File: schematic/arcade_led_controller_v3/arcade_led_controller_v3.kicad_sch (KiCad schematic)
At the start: 48 parts, among them J4 Pico_Socket_Row_2, J5 Pico_Socket_Row_1, Q1 Q_NMOS_GDS, Q2 Q_NMOS_GDS, Q3 Q_NMOS_GDS, Q4 Q_NMOS_GDS, Q5 Q_NMOS_GDS, Q6 Q_NMOS_GDS, Q7 Q_NMOS_GDS, Q8 Q_NMOS_GDS, U1 74AHCT125, U2 74AHCT125, U3 74AHCT125, U4 74AHCT125

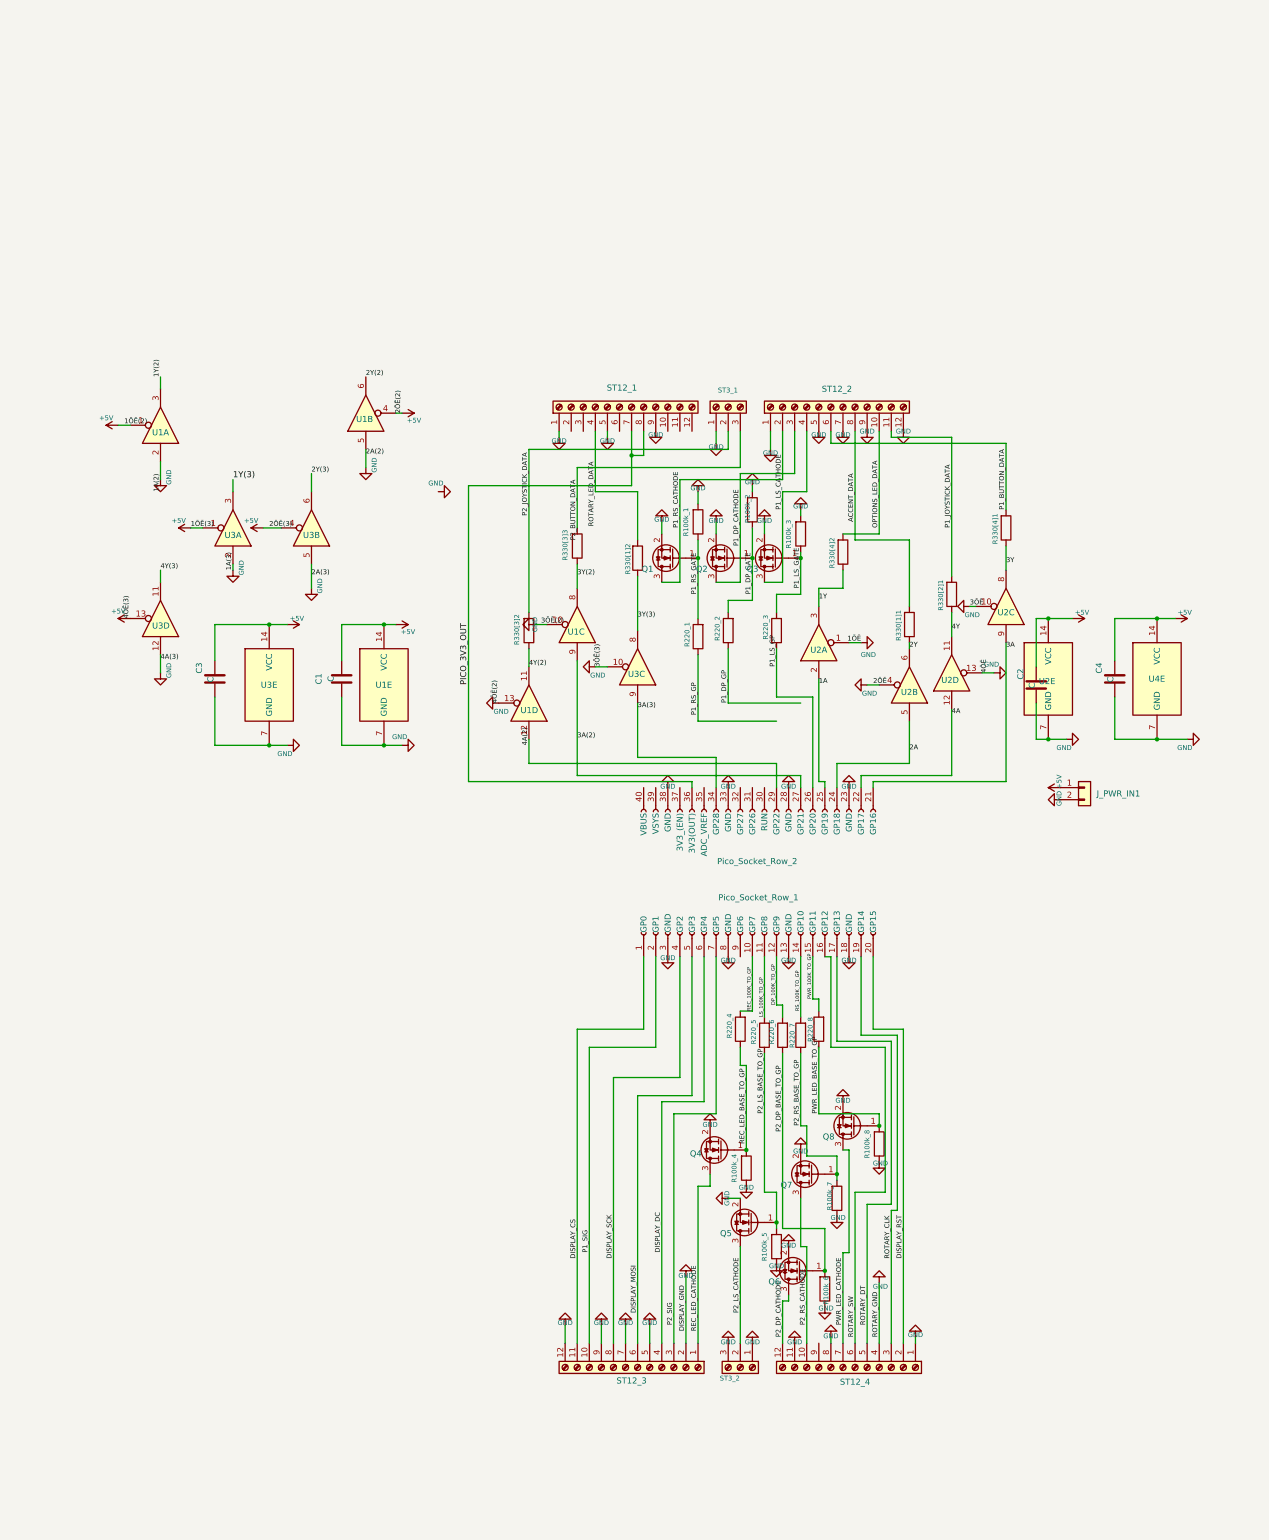
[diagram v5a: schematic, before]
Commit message: complete routing
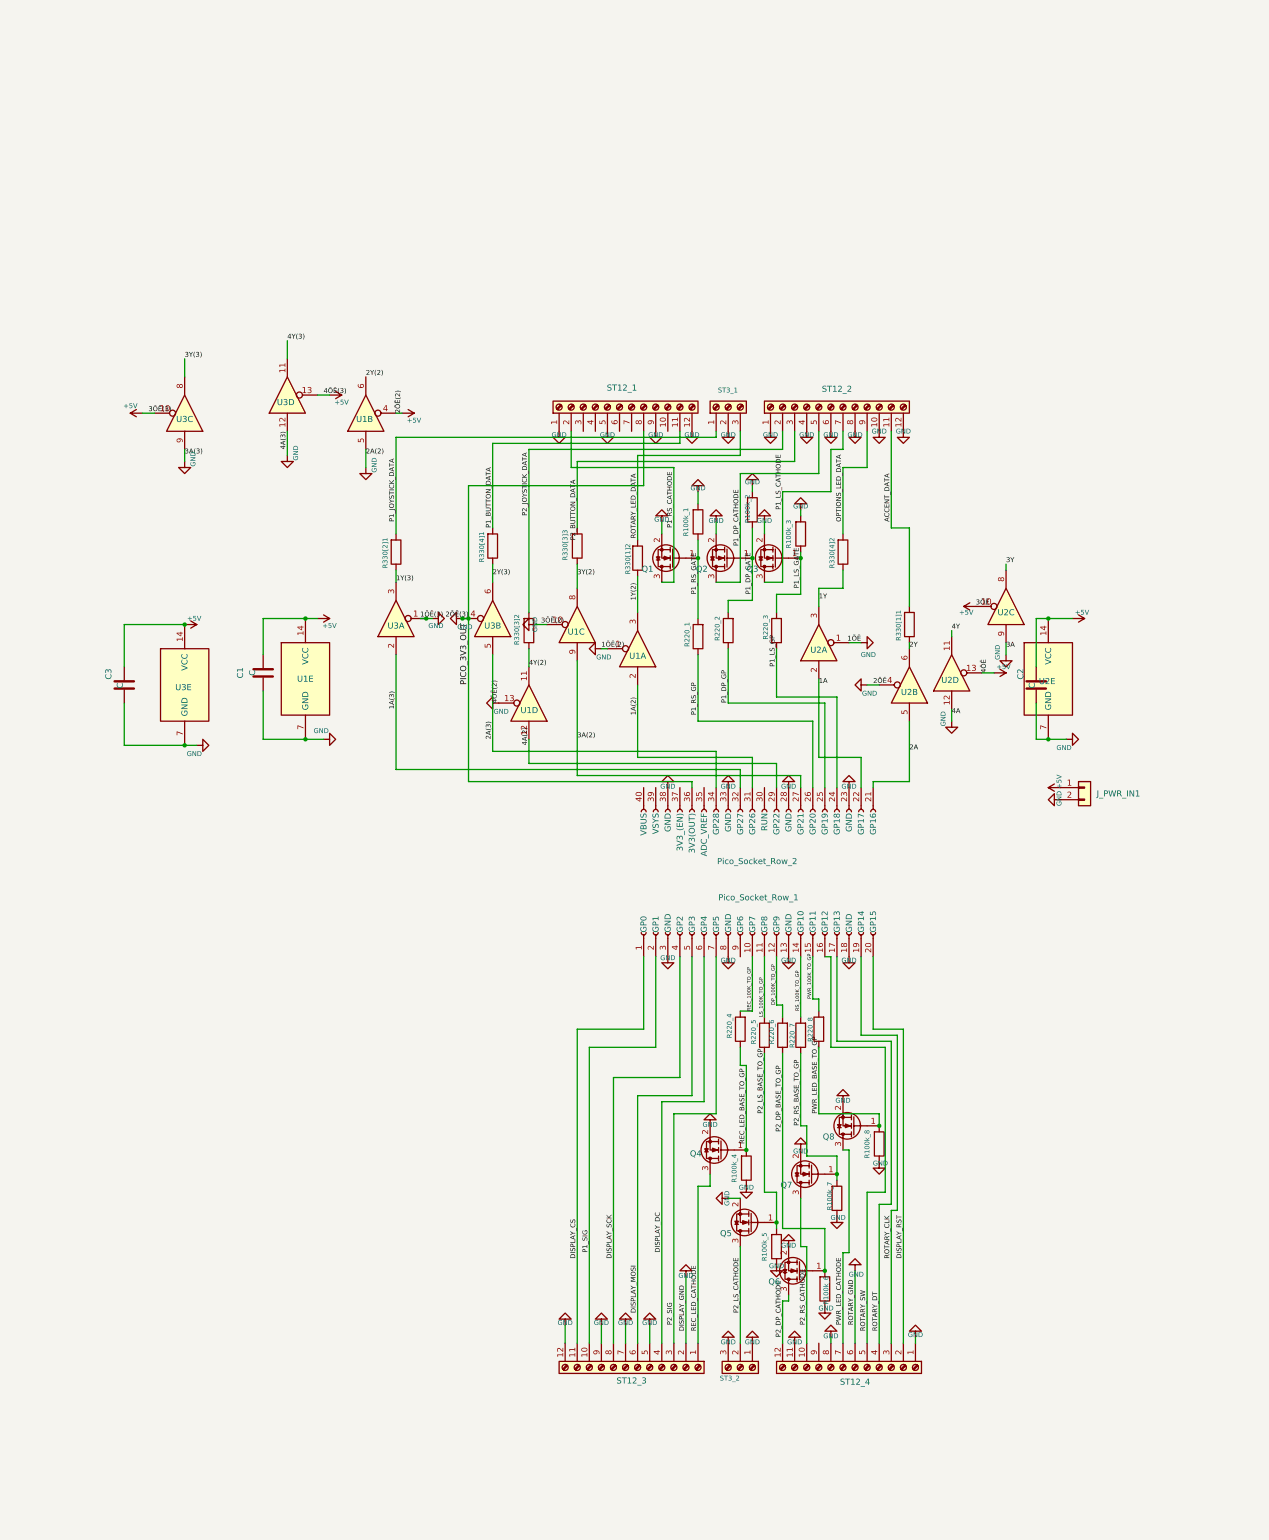
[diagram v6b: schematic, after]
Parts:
- removed C4: C, Capacitor_SMD:C_0805_2012Metric_Pad1.18x1.45mm_HandSolder, symbol Device:C
- removed U4: 74AHCT125, Package_SO:SOIC-14_3.9x8.7mm_P1.27mm, symbol 74xx:74AHCT125
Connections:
- net +5V: now also U2.10, U2.13, U3.10; no longer U1.1, U3.1, U3.4
- net 1A: now also J4.22 (GP17); no longer J4.25 (GP19)
- net 1Y(2): now also R330[1]2.1
- net 1Y(3): now also R330[2]1.1
- net 2A: now also J4.21 (GP16); no longer J4.24 (GP18)
- net 2Y(3): now also R330[4]1.1
- net 3Y: no longer R330[4]1.1
- net 3Y(3): no longer R330[1]2.1
- net 4Y: no longer R330[2]1.1
- net ACCENT_DATA: now also ST12_2.11 (Pin_11); no longer ST12_2.8 (Pin_8)
- net GND: now also J4.36 (3V3(OUT)), ST12_1.12 (Pin_12), ST12_1.8 (Pin_8), ST12_2.10 (Pin_10), ST12_2.4 (Pin_4), ST12_2.6 (Pin_6), ST12_2.8 (Pin_8), ST12_4.6 (Pin_6), ST3_1.2 (Pin_2), U1.1, U2.12, U2.9, U3.1, U3.4, U3.9; no longer ST12_2.5 (Pin_5), ST12_2.7 (Pin_7), ST12_2.9 (Pin_9), ST12_4.4 (Pin_4), ST3_1.1 (Pin_1), U1.2, U2.10, U2.13, U3.10, U3.2, U3.5
- net OPTIONS_LED_DATA: now also ST12_2.9 (Pin_9); no longer ST12_2.10 (Pin_10)
- net P1_BUTTON_DATA: now also ST12_1.11 (Pin_11); no longer ST12_2.6 (Pin_6)
- net P1_DP_CATHODE: now also ST12_2.5 (Pin_5); no longer ST12_2.3 (Pin_3)
- net P1_DP_GP: now also J4.25 (GP19)
- net P1_JOYSTICK_DATA: now also ST3_1.1 (Pin_1); no longer ST12_2.11 (Pin_11)
- net P1_LS_CATHODE: now also ST12_2.7 (Pin_7); no longer ST12_2.4 (Pin_4)
- net P1_LS_GP: now also J4.24 (GP18); no longer J4.26 (GP20)
- net P1_RS_CATHODE: now also ST12_1.2 (Pin_2); no longer ST12_2.2 (Pin_2)
- net P1_RS_GP: now also J4.26 (GP20)
- net P2_BUTTON_DATA: now also ST12_2.3 (Pin_3); no longer ST3_1.3 (Pin_3)
- net P2_JOYSTICK_DATA: now also ST12_2.2 (Pin_2); no longer ST3_1.2 (Pin_2)
- net ROTARY_DT: now also ST12_4.4 (Pin_4); no longer ST12_4.5 (Pin_5)
- net ROTARY_LED_DATA: now also ST3_1.3 (Pin_3); no longer ST12_1.4 (Pin_4)
- net ROTARY_SW: now also ST12_4.5 (Pin_5); no longer ST12_4.6 (Pin_6)
- net 1A(2): now reaches J4.31 (GP26)
- net 1A(2): now also U1.2
- net 1A(3): now reaches J4.32 (GP27)
- net 1A(3): now also U3.2
- removed net 3A: J4.21 (GP16), U2.9
- net 3A(3) renamed 2A(3)
- net 2A(3): now also U3.5; no longer U3.9
- removed net 4A: J4.22 (GP17), U2.12
- removed net PICO_3V3_OUT: J4.36 (3V3(OUT)), ST12_1.7 (Pin_7), ST12_1.8 (Pin_8)
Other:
- moved on the sheet: C1, R330[2]1, R330[4]1, U1A, U1E

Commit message: Swap some screw terminals for jst connectors, and simplify routing
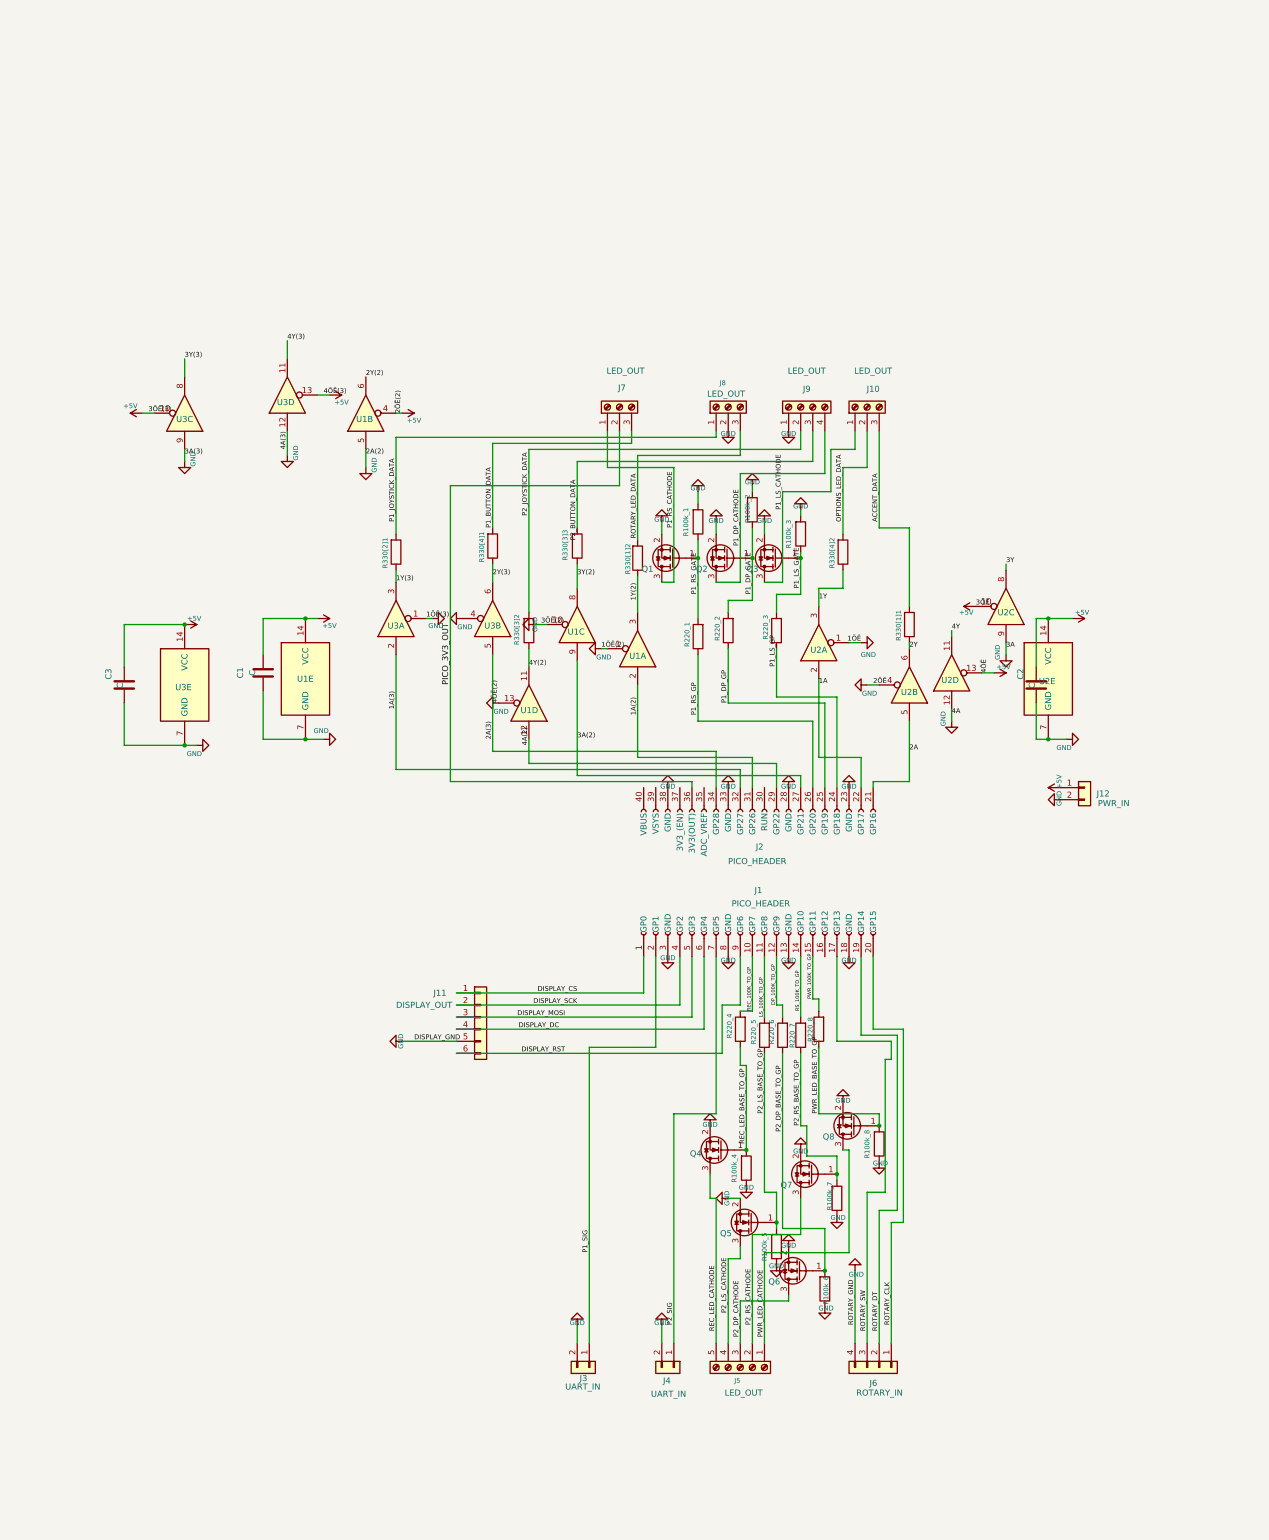
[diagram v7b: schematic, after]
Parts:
- removed ST12_3, ST12_4: Screw_Terminal_01x12, TerminalBlock_TE-Connectivity:TerminalBlock_TE_1-282834-2_1x12_P2.54mm_Horizontal, symbol Connector:Screw_Terminal_01x12
- added J10: LED_OUT, TerminalBlock_MetzConnect:TerminalBlock_MetzConnect_Type086_RT03403HBLC_1x03_P3.81mm_Horizontal, symbol Connector:Screw_Terminal_01x03
- added J11: DISPLAY_OUT, Connector_JST:JST_XH_B6B-XH-A_1x06_P2.50mm_Vertical, symbol Connector_Generic:Conn_01x06
- added J3, J4: UART_IN, Connector_JST:JST_XH_B2B-XH-A_1x02_P2.50mm_Vertical, symbol Connector_Generic:Conn_01x02
- added J6: ROTARY_IN, Connector_JST:JST_XH_B4B-XH-A_1x04_P2.50mm_Vertical, symbol Connector_Generic:Conn_01x04
- J1: renamed from J5; value Pico_Socket_Row_1 -> PICO_HEADER
- J12: renamed from J_PWR_IN1; value Conn_01x02 -> PWR_IN
- J2: renamed from J4; value Pico_Socket_Row_2 -> PICO_HEADER
- J5: renamed from ST3_2; value Screw_Terminal_01x05 -> LED_OUT; footprint TerminalBlock_TE-Connectivity:TerminalBlock_TE_282834-3_1x03_P2.54mm_Horizontal -> TerminalBlock_MetzConnect:TerminalBlock_MetzConnect_Type086_RT03405HBLC_1x05_P3.81mm_Horizontal; symbol Connector:Screw_Terminal_01x03 -> Connector:Screw_Terminal_01x05
- J7: renamed from ST12_1; value Screw_Terminal_01x12 -> LED_OUT; footprint TerminalBlock_TE-Connectivity:TerminalBlock_TE_1-282834-2_1x12_P2.54mm_Horizontal -> TerminalBlock_MetzConnect:TerminalBlock_MetzConnect_Type086_RT03403HBLC_1x03_P3.81mm_Horizontal; symbol Connector:Screw_Terminal_01x12 -> Connector:Screw_Terminal_01x03
- J8: renamed from ST3_1; value Screw_Terminal_01x05 -> LED_OUT; footprint TerminalBlock_TE-Connectivity:TerminalBlock_TE_282834-3_1x03_P2.54mm_Horizontal -> TerminalBlock_MetzConnect:TerminalBlock_MetzConnect_Type086_RT03403HBLC_1x03_P3.81mm_Horizontal
- J9: renamed from ST12_2; value Screw_Terminal_01x12 -> LED_OUT; footprint TerminalBlock_TE-Connectivity:TerminalBlock_TE_1-282834-2_1x12_P2.54mm_Horizontal -> TerminalBlock_MetzConnect:TerminalBlock_MetzConnect_Type086_RT03404HBLC_1x04_P3.81mm_Horizontal; symbol Connector:Screw_Terminal_01x12 -> Connector:Screw_Terminal_01x04
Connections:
- net ACCENT_DATA: now also J10.3 (Pin_3); no longer J9.11 (Pin_11)
- net DISPLAY_CS: now also J11.1 (Pin_1)
- net DISPLAY_DC: now also J11.4 (Pin_4)
- net DISPLAY_MOSI: now also J11.3 (Pin_3)
- net DISPLAY_RST: now also J1.9 (GP6), J11.6 (Pin_6); no longer J1.20 (GP15)
- net DISPLAY_SCK: now also J11.2 (Pin_2)
- net GND: now also J11.5 (Pin_5), J3.2 (Pin_2), J4.2 (Pin_2), J6.4 (Pin_4); no longer J2.36 (3V3(OUT)), J5.1 (Pin_1), J5.3 (Pin_3), J7.1 (Pin_1), J7.12 (Pin_12), J7.5 (Pin_5), J7.8 (Pin_8), J7.9 (Pin_9), J9.10 (Pin_10), J9.12 (Pin_12), J9.4 (Pin_4), J9.6 (Pin_6), J9.8 (Pin_8)
- net OPTIONS_LED_DATA: now also J10.2 (Pin_2); no longer J9.9 (Pin_9)
- net P1_BUTTON_DATA: now also J7.3 (Pin_3); no longer J7.11 (Pin_11)
- net P1_DP_CATHODE: now also J9.4 (Pin_4); no longer J9.5 (Pin_5)
- net P1_LS_CATHODE: now also J10.1 (Pin_1); no longer J9.7 (Pin_7)
- net P1_RS_CATHODE: now also J7.1 (Pin_1); no longer J7.2 (Pin_2)
- net P1_SIG: now also J3.1 (Pin_1)
- net P2_DP_CATHODE: now also J5.3 (Pin_3)
- net P2_LS_CATHODE: now also J5.4 (Pin_4); no longer J5.2 (Pin_2)
- net P2_RS_CATHODE: now also J5.2 (Pin_2)
- net P2_SIG: now also J4.1 (Pin_1)
- net PWR_LED_CATHODE: now also J5.1 (Pin_1)
- net REC_LED_CATHODE: now also J5.5 (Pin_5)
- net ROTARY_CLK: now also J1.20 (GP15), J6.1 (Pin_1); no longer J1.19 (GP14)
- net ROTARY_DT: now also J1.19 (GP14), J6.2 (Pin_2); no longer J1.17 (GP13)
- net ROTARY_SW: now also J1.17 (GP13), J6.3 (Pin_3); no longer J1.16 (GP12)
- new net PICO_3V3_OUT: J2.36 (3V3(OUT)), J7.2 (Pin_2)
